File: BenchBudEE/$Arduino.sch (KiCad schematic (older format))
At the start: 16 parts

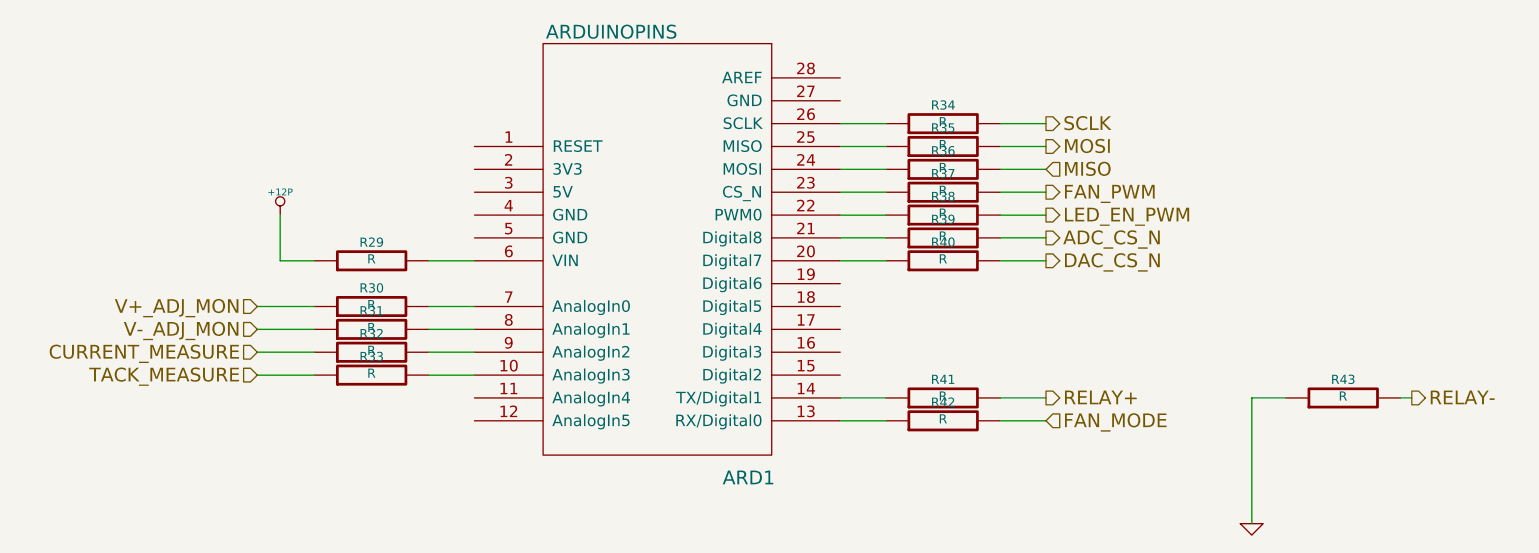
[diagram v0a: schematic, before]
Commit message: Parts added to thermocouple module. Relay & thermocouple rough placement.
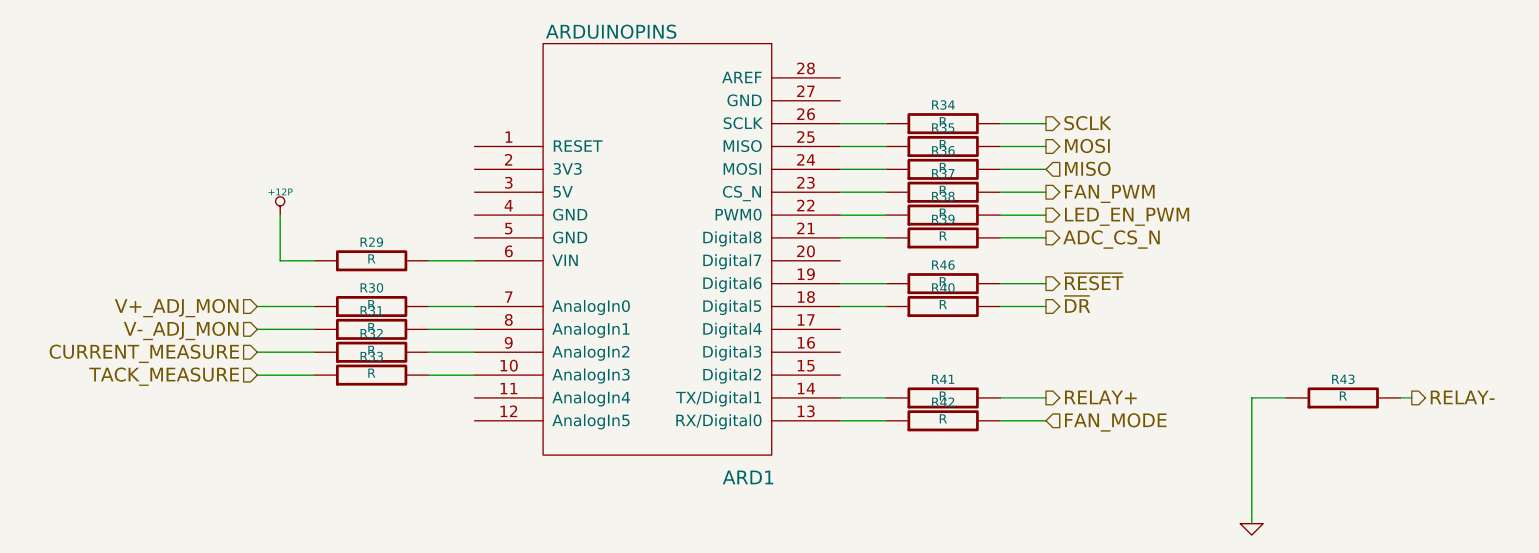
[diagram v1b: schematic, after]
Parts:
- added R46: R, ~, symbol R
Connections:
- net at ARD1.18 (Digital5): now also R40.1
- net at ARD1.19 (Digital6): now also R46.1
- net at ARD1.20 (Digital7): no longer R40.1
- net DAC_CS_N renamed ~DR
- new net ~RESET: R46.2
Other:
- moved on the sheet: R40
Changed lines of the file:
@@
 Sheet 9 9
 Title ""
-Date "20 feb 2014"
+Date "21 feb 2014"
 Rev ""
 Comp ""
@@
 Text HLabel 7700 1800 2    60   Output ~ 0
 SCLK
-Text HLabel 7700 2400 2    60   Output ~ 0
-DAC_CS_N
+Text HLabel 7700 2600 2    60   Output ~ 0
+~DR
 Text HLabel 7700 3000 2    60   Output ~ 0
 RELAY+
@@
 	7000 3000 6800 3000
 $Comp
-L GND #PWR052
+L GND #PWR62
 U 1 1 52F67CCE
 P 8600 3550
-F 0 "#PWR052" H 8600 3550 30  0001 C CNN
+F 0 "#PWR62" H 8600 3550 30  0001 C CNN
 F 1 "GND" H 8600 3480 30  0001 C CNN
 F 2 "" H 8600 3550 60  0000 C CNN
@@
 L R R40
 U 1 1 52F82098
-P 7250 2400
-F 0 "R40" V 7330 2400 40  0000 C CNN
-F 1 "R" V 7257 2401 40  0000 C CNN
-F 2 "~" V 7180 2400 30  0000 C CNN
-F 3 "~" H 7250 2400 30  0000 C CNN
-	1    7250 2400
-	0    -1   -1   0
-$EndComp
-Wire Wire Line
-	7500 2400 7700 2400
-Wire Wire Line
-	7000 2400 6800 2400
+P 7250 2600
+F 0 "R40" V 7330 2600 40  0000 C CNN
+F 1 "R" V 7257 2601 40  0000 C CNN
+F 2 "~" V 7180 2600 30  0000 C CNN
+F 3 "~" H 7250 2600 30  0000 C CNN
+	1    7250 2600
+	0    -1   -1   0
+$EndComp
+Wire Wire Line
+	7500 2600 7700 2600
+Wire Wire Line
+	7000 2600 6800 2600
 Text HLabel 7700 3100 2    60   Input ~ 0
 FAN_MODE
@@
 	5000 2400 5200 2400
 $Comp
-L +12P #PWR053
+L +12P #PWR61
 U 1 1 52F8274D
 P 4350 2200
-F 0 "#PWR053" H 4350 2170 30  0001 C CNN
+F 0 "#PWR61" H 4350 2170 30  0001 C CNN
 F 1 "+12P" H 4350 2300 30  0000 C CNN
 F 2 "" H 4350 2200 60  0000 C CNN
@@
 Wire Wire Line
 	4350 2400 4500 2400
+$Comp
+L R R46
+U 1 1 5307173C
+P 7250 2500
+F 0 "R46" V 7330 2500 40  0000 C CNN
+F 1 "R" V 7257 2501 40  0000 C CNN
+F 2 "~" V 7180 2500 30  0000 C CNN
+F 3 "~" H 7250 2500 30  0000 C CNN
+	1    7250 2500
+	0    -1   -1   0
+$EndComp
+Text HLabel 7700 2500 2    60   Output ~ 0
+~RESET
+Wire Wire Line
+	6800 2500 7000 2500
+Wire Wire Line
+	7500 2500 7700 2500
 $EndSCHEMATC
